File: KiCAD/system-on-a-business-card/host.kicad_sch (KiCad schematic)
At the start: 28 parts, among them J4 Micro_SD_Card, Q1 2N7002K, Q2 2N7002K, SW2 SW_Push, U2 ESP32-C3, U3 ZD25WQ32C, Y1 40MHz

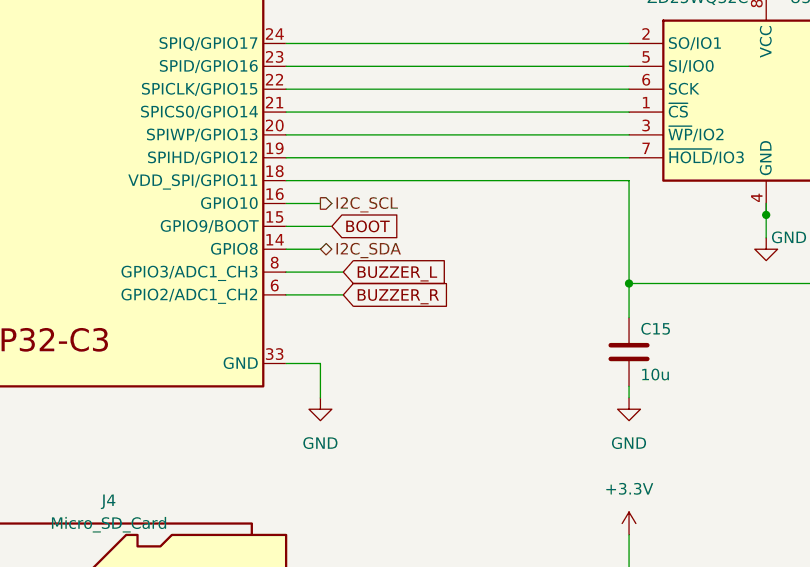
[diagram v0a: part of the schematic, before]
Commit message: #10: finished routing except PCB antenna
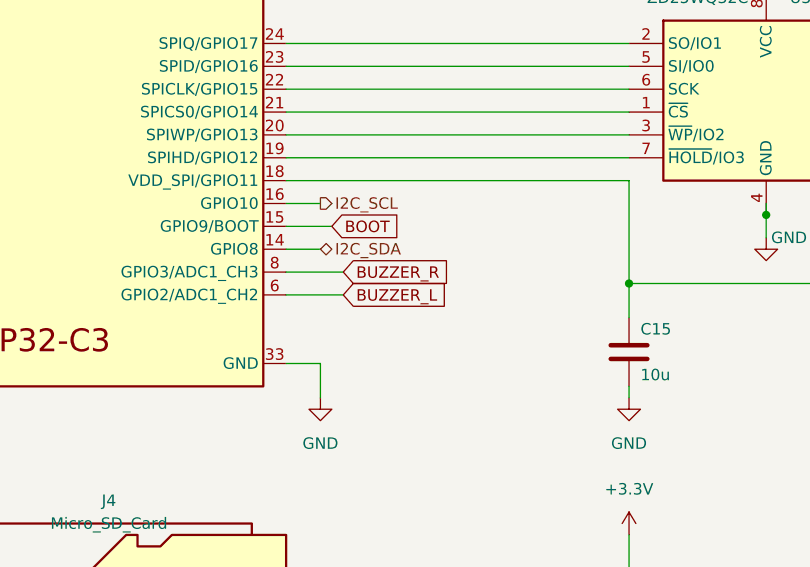
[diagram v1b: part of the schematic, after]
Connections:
- net BUZZER_L: now also U2.6 (GPIO2/ADC1_CH2); no longer U2.8 (GPIO3/ADC1_CH3)
- net BUZZER_R: now also U2.8 (GPIO3/ADC1_CH3); no longer U2.6 (GPIO2/ADC1_CH2)
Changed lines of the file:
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@@
     )
   )
-  (global_label "BUZZER_R" (shape input) (at 189.23 77.47 0) (fields_autoplaced)
+  (global_label "BUZZER_R" (shape input) (at 189.23 74.93 0) (fields_autoplaced)
     (effects (font (size 1.27 1.27)) (justify left))
-    (property "Intersheetrefs" "${INTERSHEET_REFS}" (at 201.8913 77.47 0)
+    (property "Intersheetrefs" "${INTERSHEET_REFS}" (at 201.8913 74.93 0)
       (effects (font (size 1.27 1.27)) (justify left) hide)
     )
@@
     )
   )
-  (global_label "BUZZER_L" (shape input) (at 189.23 74.93 0) (fields_autoplaced)
+  (global_label "BUZZER_L" (shape input) (at 189.23 77.47 0) (fields_autoplaced)
     (effects (font (size 1.27 1.27)) (justify left))
-    (property "Intersheetrefs" "${INTERSHEET_REFS}" (at 201.6494 74.93 0)
+    (property "Intersheetrefs" "${INTERSHEET_REFS}" (at 201.6494 77.47 0)
       (effects (font (size 1.27 1.27)) (justify left) hide)
     )

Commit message: #10: finished initial routing
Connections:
- net SDcard_DET: now reaches J4.9 (DET)
- no-connect marks 4 -> 3
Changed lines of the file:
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@@
   (no_connect (at 139.7 111.76))
   (no_connect (at 139.7 109.22))
-  (no_connect (at 139.7 132.08))
   (no_connect (at 182.88 134.62))
   (wire (pts (xy 73.66 77.47) (xy 73.66 85.09))
@@
     (stroke (width 0) (type default))
   )
-  (wire (pts (xy 125.73 129.54) (xy 125.73 124.46))
-    (stroke (width 0) (type default))
-  )
-  (wire (pts (xy 125.73 124.46) (xy 139.7 124.46))
+  (wire (pts (xy 119.38 129.54) (xy 119.38 124.46))
+    (stroke (width 0) (type default))
+  )
+  (wire (pts (xy 119.38 124.46) (xy 139.7 124.46))
     (stroke (width 0) (type default))
   )
@@
   )
   (wire (pts (xy 52.07 57.15) (xy 58.42 57.15))
+    (stroke (width 0) (type default))
+  )
+  (wire (pts (xy 134.62 132.08) (xy 139.7 132.08))
     (stroke (width 0) (type default))
   )
@@
   (hierarchical_label "USB_D-" (shape bidirectional) (at 186.69 41.91 0) (fields_autoplaced)
     (effects (font (size 1.27 1.27)) (justify left))
+  )
+  (hierarchical_label "SDcard_DET" (shape input) (at 134.62 132.08 180) (fields_autoplaced)
+    (effects (font (size 1.27 1.27)) (justify right))
   )
   (hierarchical_label "UART_RXD" (shape output) (at 186.69 34.29 0) (fields_autoplaced)
@@
     )
   )
-  (symbol (lib_id "power:GND") (at 125.73 129.54 0) (mirror y) (unit 1)
+  (symbol (lib_id "power:GND") (at 119.38 129.54 0) (mirror y) (unit 1)
     (in_bom yes) (on_board yes) (dnp no) (fields_autoplaced)
-    (property "Reference" "#PWR055" (at 125.73 135.89 0)
-      (effects (font (size 1.27 1.27)) hide)
-    )
-    (property "Value" "GND" (at 125.73 134.62 0)
-      (effects (font (size 1.27 1.27)))
-    )
-    (property "Footprint" "" (at 125.73 129.54 0)
-      (effects (font (size 1.27 1.27)) hide)
-    )
-    (property "Datasheet" "" (at 125.73 129.54 0)
-      (effects (font (size 1.27 1.27)) hide)
-    )
+    (property "Reference" "#PWR055" (at 119.38 135.89 0)
+      (effects (font (size 1.27 1.27)) hide)
+    )
+    (property "Value" "GND" (at 119.38 134.62 0)
+      (effects (font (size 1.27 1.27)))
+    )
+    (property "Footprint" "" (at 119.38 129.54 0)
+      (effects (font (size 1.27 1.27)) hide)
+    )
+    (property "Datasheet" "" (at 119.38 129.54 0)
+      (effects (font (size 1.27 1.27)) hide)
+    )

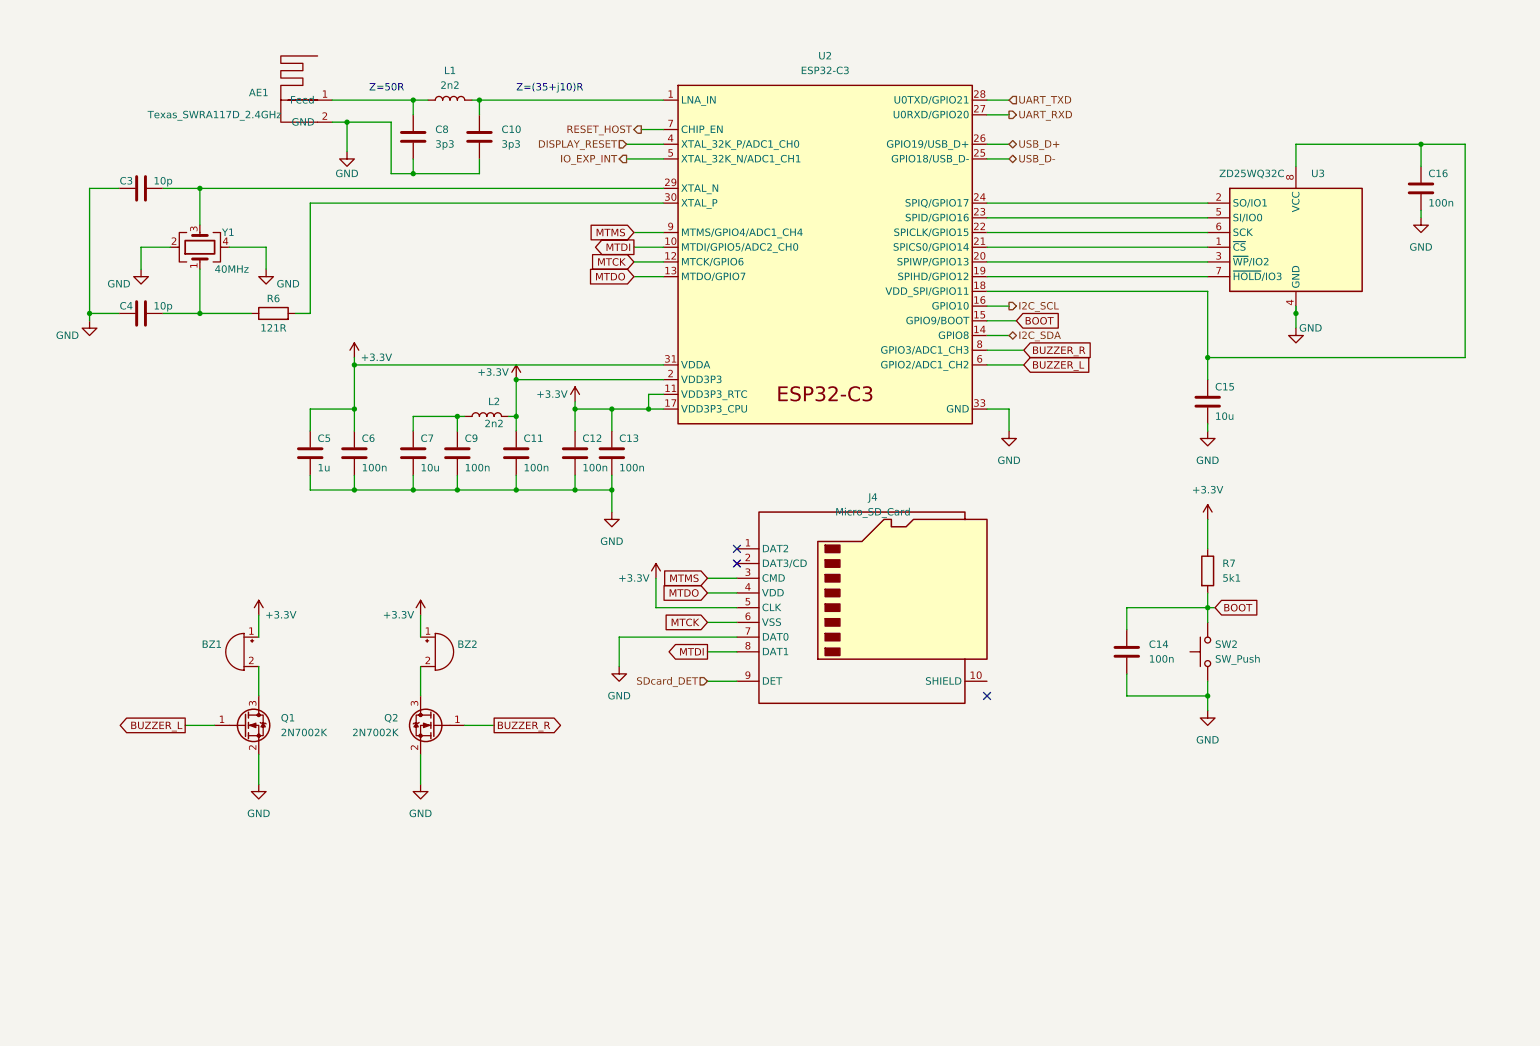
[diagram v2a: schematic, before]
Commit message: #10: added pull-ups to SD-Card connection, tweaks in layout
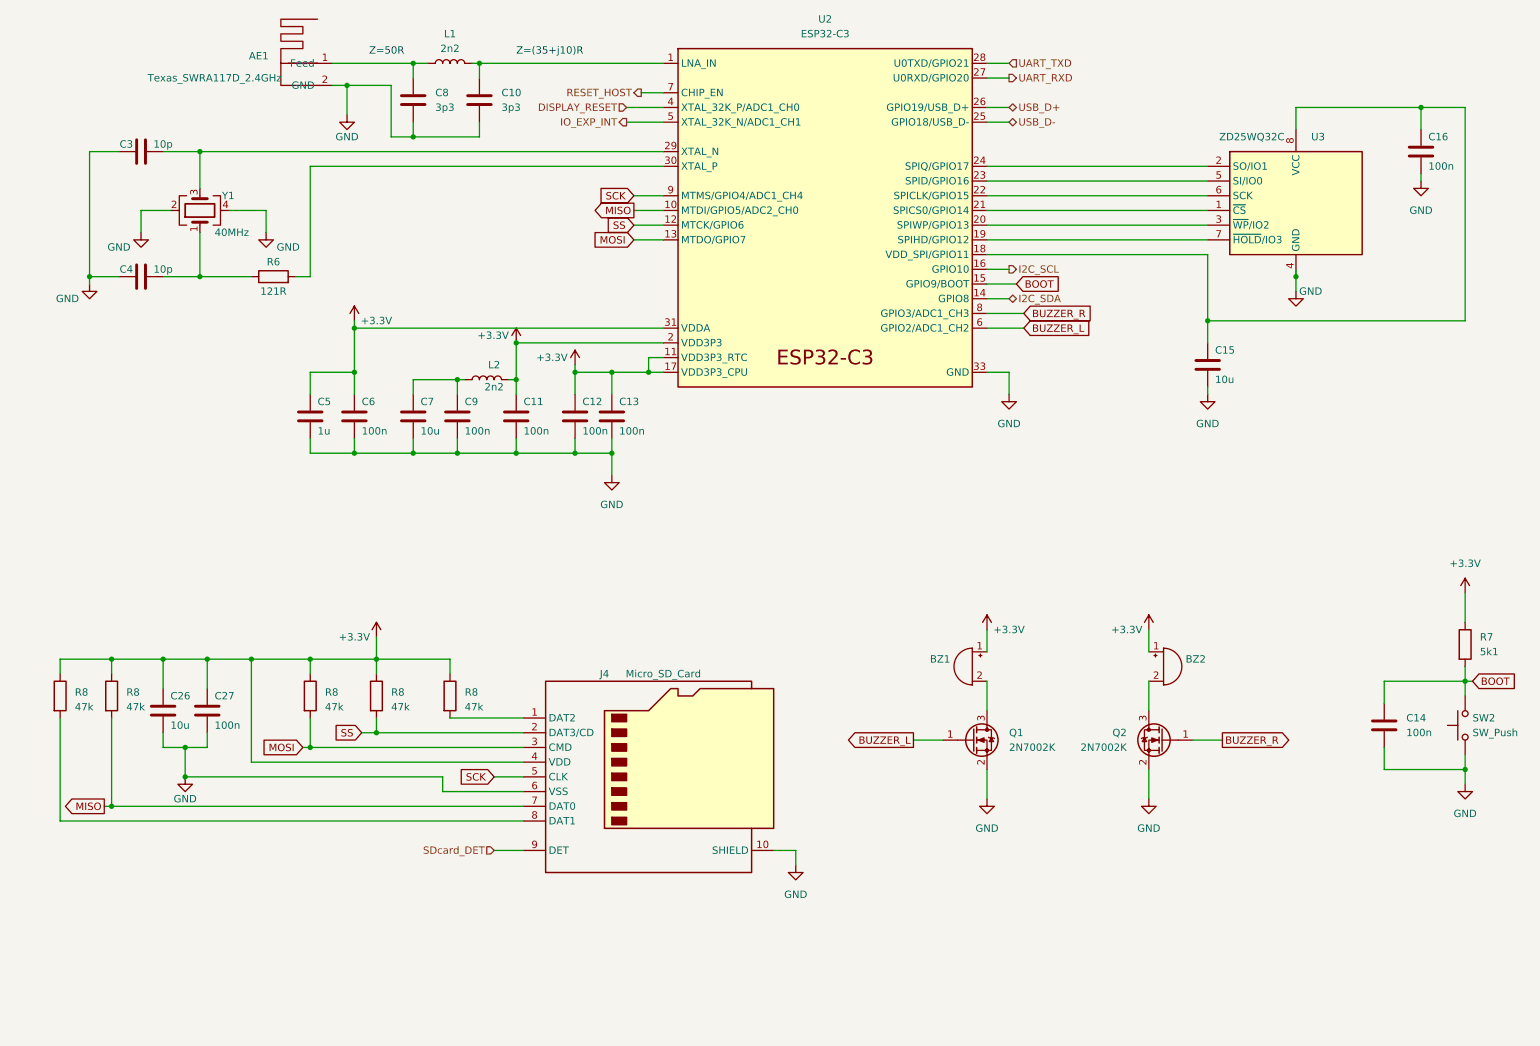
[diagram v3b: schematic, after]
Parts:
- added C26: 10u, Capacitor_SMD:C_0402_1005Metric_Pad0.74x0.62mm_HandSolder, symbol Device:C
- added C27: 100n, Capacitor_SMD:C_0402_1005Metric_Pad0.74x0.62mm_HandSolder, symbol Device:C
- added R8 (x5): 47k, Resistor_SMD:R_0402_1005Metric_Pad0.72x0.64mm_HandSolder, symbol Device:R
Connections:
- net +3.3V: now also J4.4 (VDD), C26.1, C27.1, R8.1, R8.1, R8.1, R8.1, R8.1; no longer J4.5 (CLK)
- net GND: now also J4.10 (SHIELD), J4.6 (VSS), C26.2, C27.2; no longer J4.7 (DAT0)
- net at J4.1 (DAT2): now also R8.2
- net SS: now reaches J4.2 (DAT3/CD)
- net SS: now also U2.12 (MTCK/GPIO6), R8.2
- removed net MTCK: J4.6 (VSS), U2.12 (MTCK/GPIO6)
- net MTDI: no longer names the net of J4.8 (DAT1)
- net MTDI: now also R8.2; no longer U2.10 (MTDI/GPIO5/ADC2_CH0)
- net MTDO renamed MOSI
- net MOSI: now also J4.3 (CMD), R8.2; no longer J4.4 (VDD)
- net MTMS renamed SCK
- net SCK: now also J4.5 (CLK); no longer J4.3 (CMD)
- new net MISO: J4.7 (DAT0), R8.2, U2.10 (MTDI/GPIO5/ADC2_CH0)
- no-connect marks 3 -> 0
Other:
- moved on the sheet: AE1, BZ1, BZ2, C10, C11, C12, C13, C14, C15, C16, C3, C4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

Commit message: #10: connected display reset to GPIO Expander
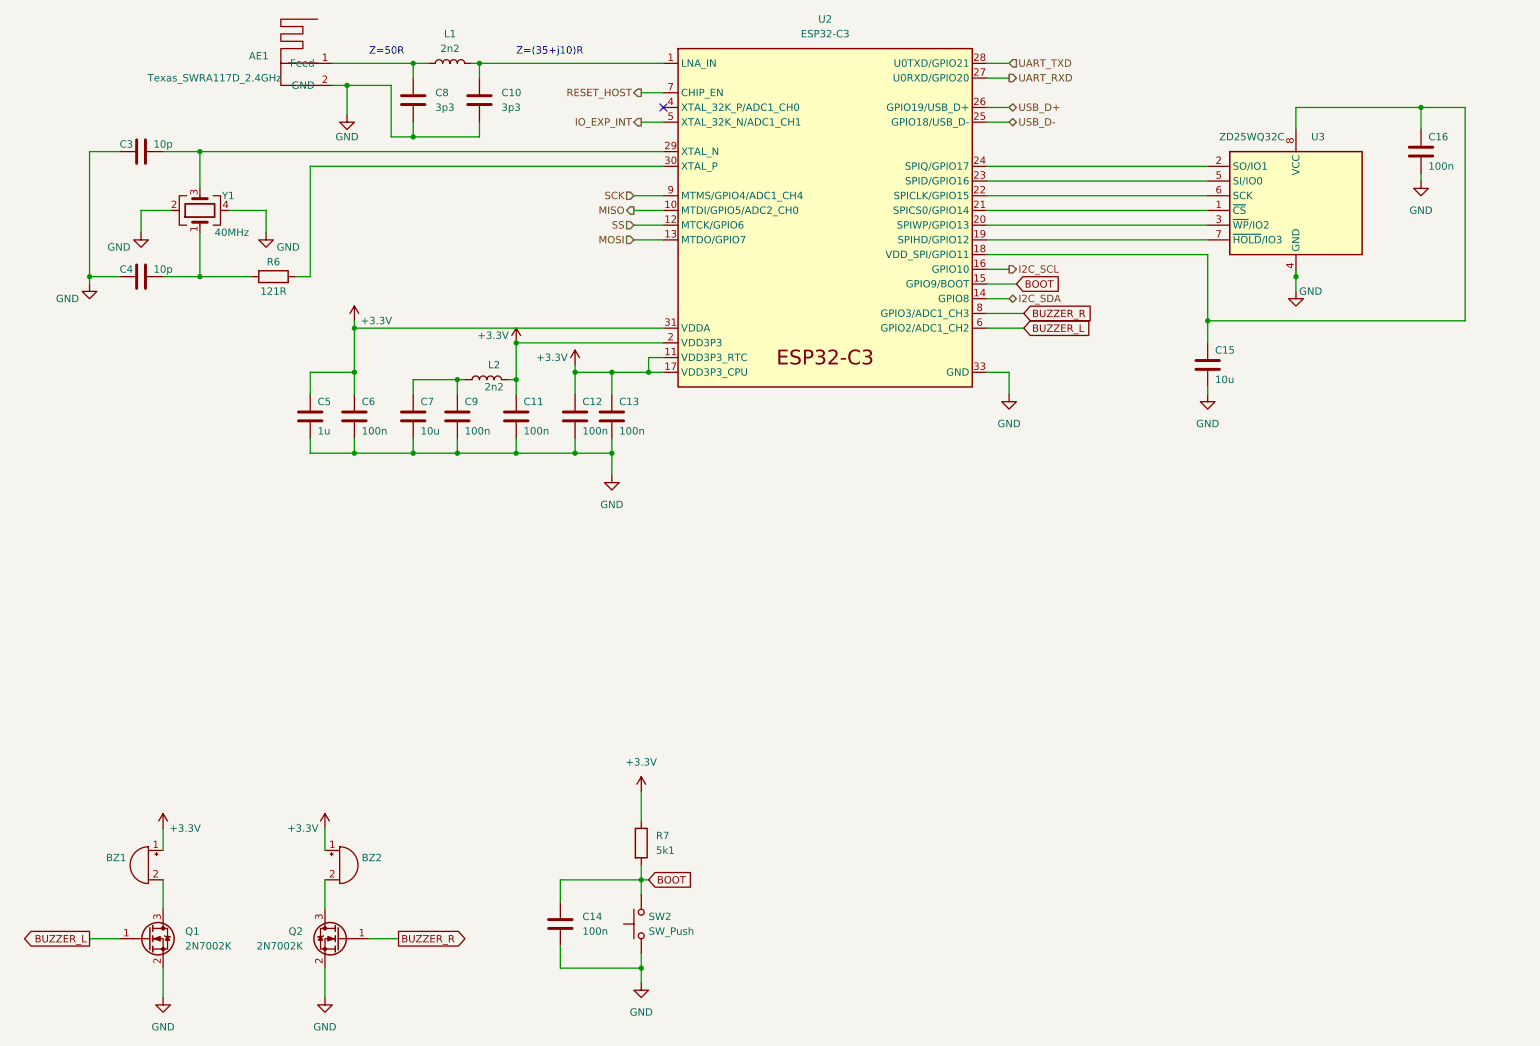
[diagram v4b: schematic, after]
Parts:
- removed C26: 10u, Capacitor_SMD:C_0402_1005Metric_Pad0.74x0.62mm_HandSolder, symbol Device:C
- removed C27: 100n, Capacitor_SMD:C_0402_1005Metric_Pad0.74x0.62mm_HandSolder, symbol Device:C
- removed J4: Micro_SD_Card, Prj_connector_card:microSD_HC_Hanbo_Electronic_TF-018B-H15, symbol Connector:Micro_SD_Card_Det1
- removed R8 (x5): 47k, Resistor_SMD:R_0402_1005Metric_Pad0.72x0.64mm_HandSolder, symbol Device:R
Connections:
- net DISPLAY_RESET: no longer names the net of U2.4 (XTAL_32K_P/ADC1_CH0)
- no-connect marks 0 -> 1
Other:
- moved on the sheet: BZ1, BZ2, C14, Q1, Q2, R7, SW2
